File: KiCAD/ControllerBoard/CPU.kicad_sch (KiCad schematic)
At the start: 41 parts, among them P1 CONN_LED, Q1 IRLML2402, U1 SAME70N21, Y1 12MHz

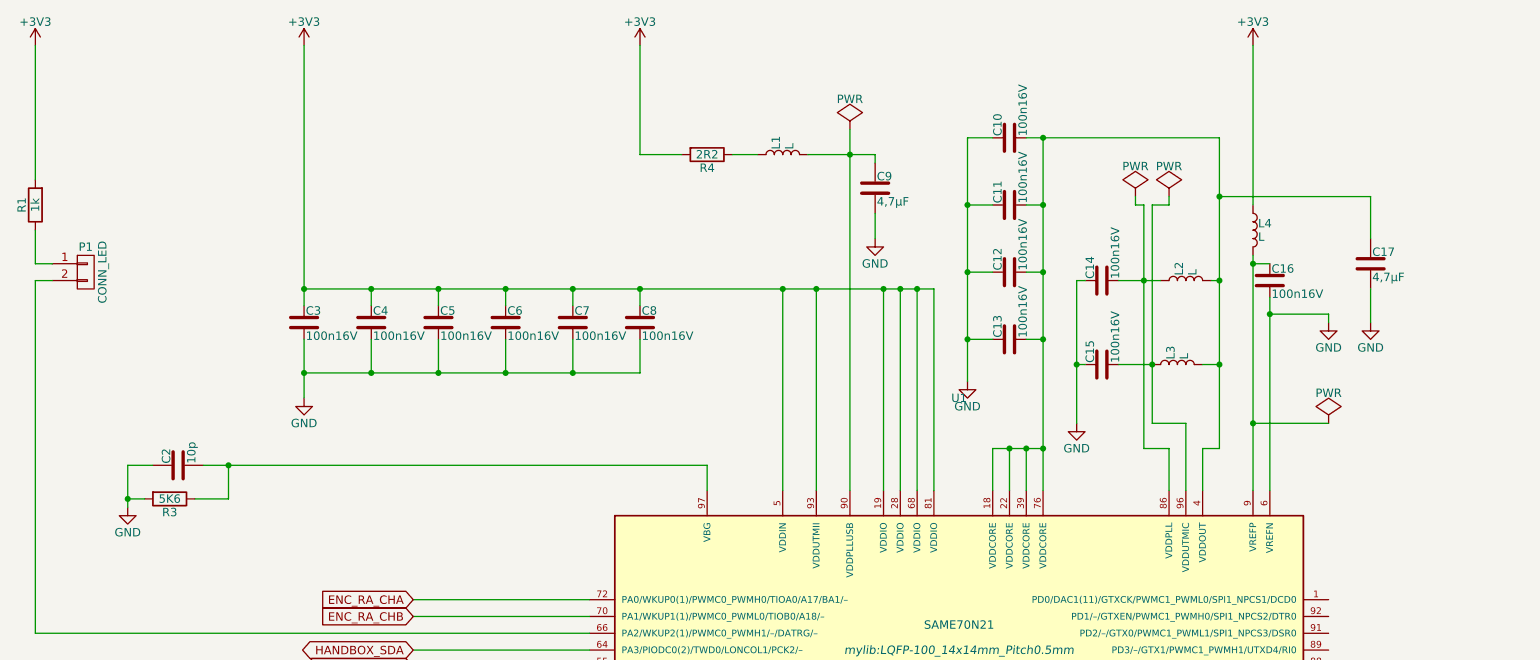
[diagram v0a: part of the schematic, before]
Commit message: CPU symbol changed, all pins on one page
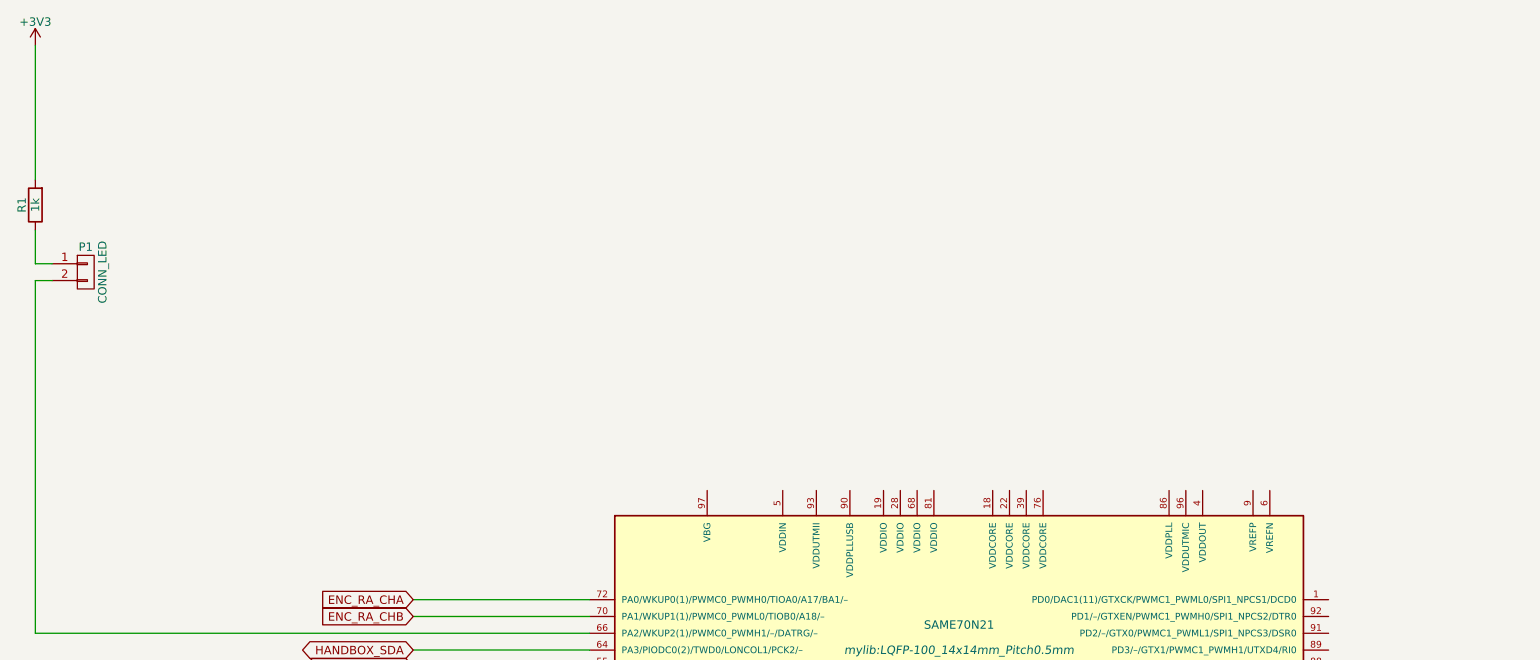
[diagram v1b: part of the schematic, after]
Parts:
- removed C10, C11, C12, C13, C14, C15, C16, C3, C4, C5, C6, C7, C8: 100n16V, ATSAME70:C_0402, symbol ATSAME70:C_100n_16V_0402
- removed C17, C9: 4,7µF, mylib:C_1206, symbol ATSAME70:C
- removed C2: 10p, mylib:C_1206, symbol ATSAME70:C
- removed L1: L, mylib:L_Chip_1210, symbol ATSAME70:L
- removed L2, L3, L4: L, mylib:C_1207_Reflow, symbol ATSAME70:L
- removed R3: 5K6, ATSAME70:R_0805, symbol ATSAME70:R_5K6_0603
- removed R4: 2R2, mylib:R_1206, symbol ATSAME70:R
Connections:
- net +3V3: no longer U1.19 (VDDIO), U1.28 (VDDIO), U1.5 (VDDIN), U1.68 (VDDIO), U1.81 (VDDIO), U1.93 (VDDUTMII)
- net GND: no longer U1.6 (VREFN)
- now unconnected: U1.18 (VDDCORE), U1.22 (VDDCORE), U1.39 (VDDCORE), U1.4 (VDDOUT), U1.76 (VDDCORE)
